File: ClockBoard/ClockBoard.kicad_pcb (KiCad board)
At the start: 2 copper layers, 43.2 x 55.9 mm, 25 parts, among them J1 Conn_01x03, J2 ClockBoard, J3 Mini USB, J4 USB Solder Pads, SW1 SW_Push, U1 ATMEGA328P, U2 UltimateGPSBreakout, U3 FT232RL, Y1 Crystal

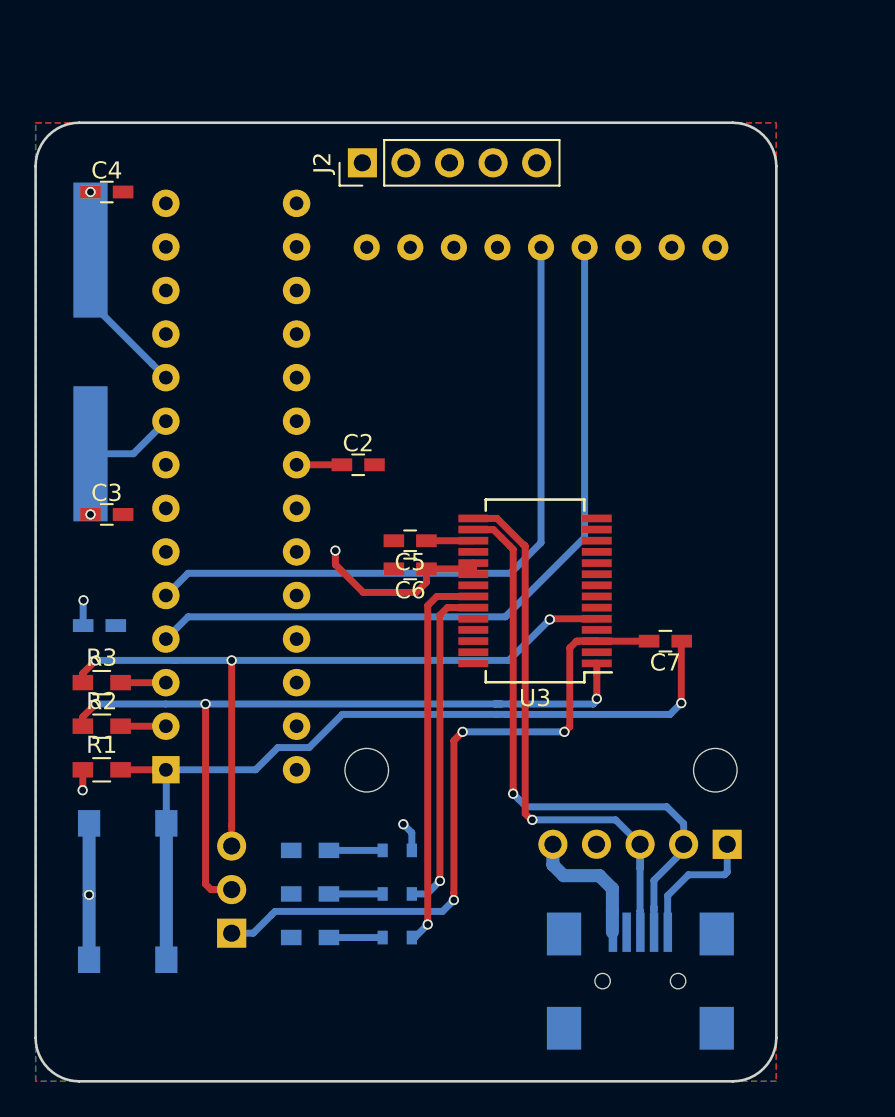
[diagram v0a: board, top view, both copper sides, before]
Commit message: Made Clock Board
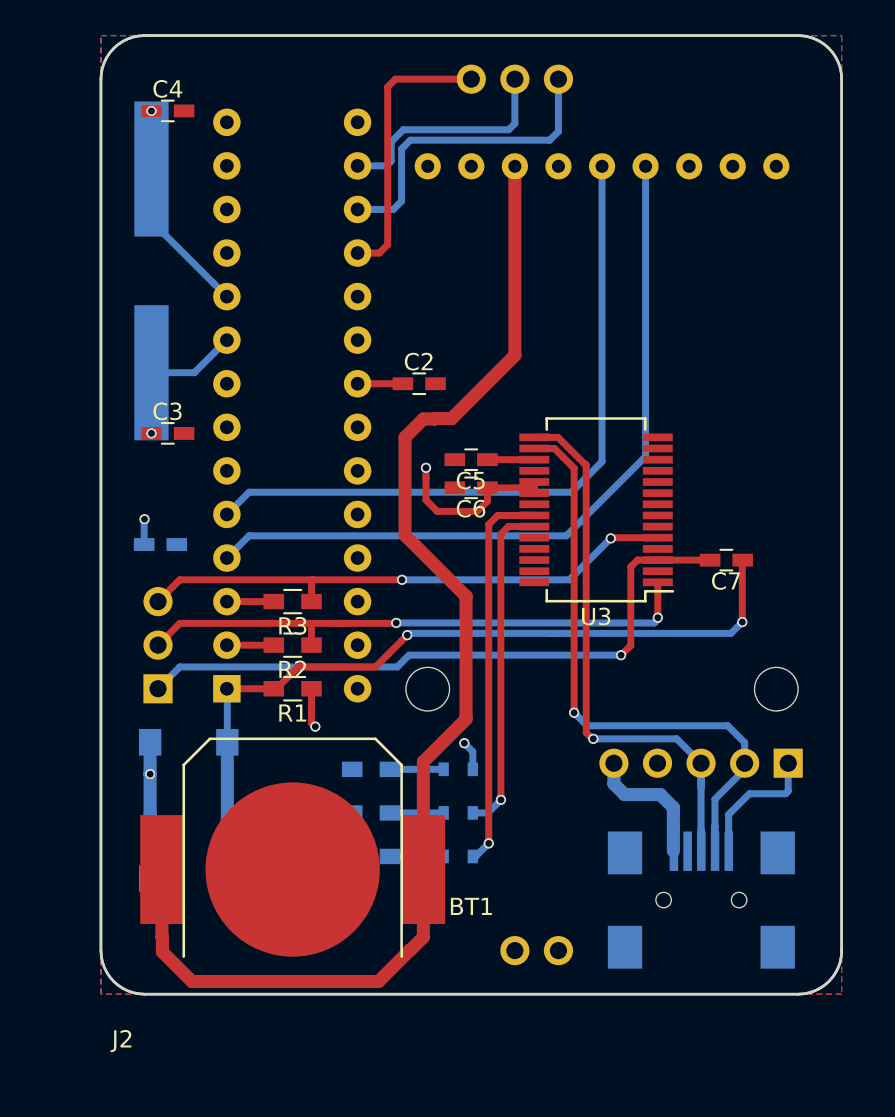
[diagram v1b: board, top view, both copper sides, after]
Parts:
- added BT1: Battery_Cell, Project_Library:CR1220_Battery_Holder, F.Cu at (126.7, 119.7)
- J2: footprint Pin_Headers:Pin_Header_Straight_1x05_Pitch2.54mm -> Project_Library:Clock_Board
- moved J2 50.8 mm to (123.2, 127.0), turned to 0 degrees
- moved J1 14.9 mm to (126.5, 109.2)
- moved R1 12.1 mm to (134.4, 109.2), turned to 180 degrees
- moved R2 12.1 mm to (134.4, 106.7), turned to 180 degrees
- moved R3 12.1 mm to (134.4, 104.1), turned to 180 degrees
- moved C5 5.91 mm to (144.8, 95.8)
- moved C7 5.91 mm to (159.6, 101.7)
- moved D2 5.91 mm to (144.0, 116.4)
- moved J3 5.91 mm to (158.2, 121.5)
- moved J4 5.91 mm to (163.3, 113.5)
- moved SW1 5.91 mm to (131.6, 113.3)
- moved U2 5.91 mm to (162.6, 78.7)
- moved C1 5.91 mm to (126.7, 100.8)
- moved C3 5.91 mm to (127.1, 94.3)
- moved C4 5.91 mm to (127.1, 75.5)
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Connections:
- U1 pad 16: (no net) -> CS
- U1 pad 17: (no net) -> CLK
- U1 pad 18: (no net) -> DIN
- U2 pad 3: (no net) -> VBat
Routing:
- net VBat: track 0.00 -> 72.9 mm
- net CLK: track 0.00 -> 18.4 mm
- net DIN: track 0.00 -> 16.2 mm
- net CS: track 0.00 -> 13.4 mm
- net IC_RX: track 45.7 -> 33.9 mm, vias 3 -> 2
- net IC_TX: track 42.6 -> 32.0 mm, vias 3 -> 2
- net Reset: track 49.0 -> 46.4 mm, vias 1 -> 2
- net RTS: track 39.5 -> 38.0 mm, vias 3 -> 1

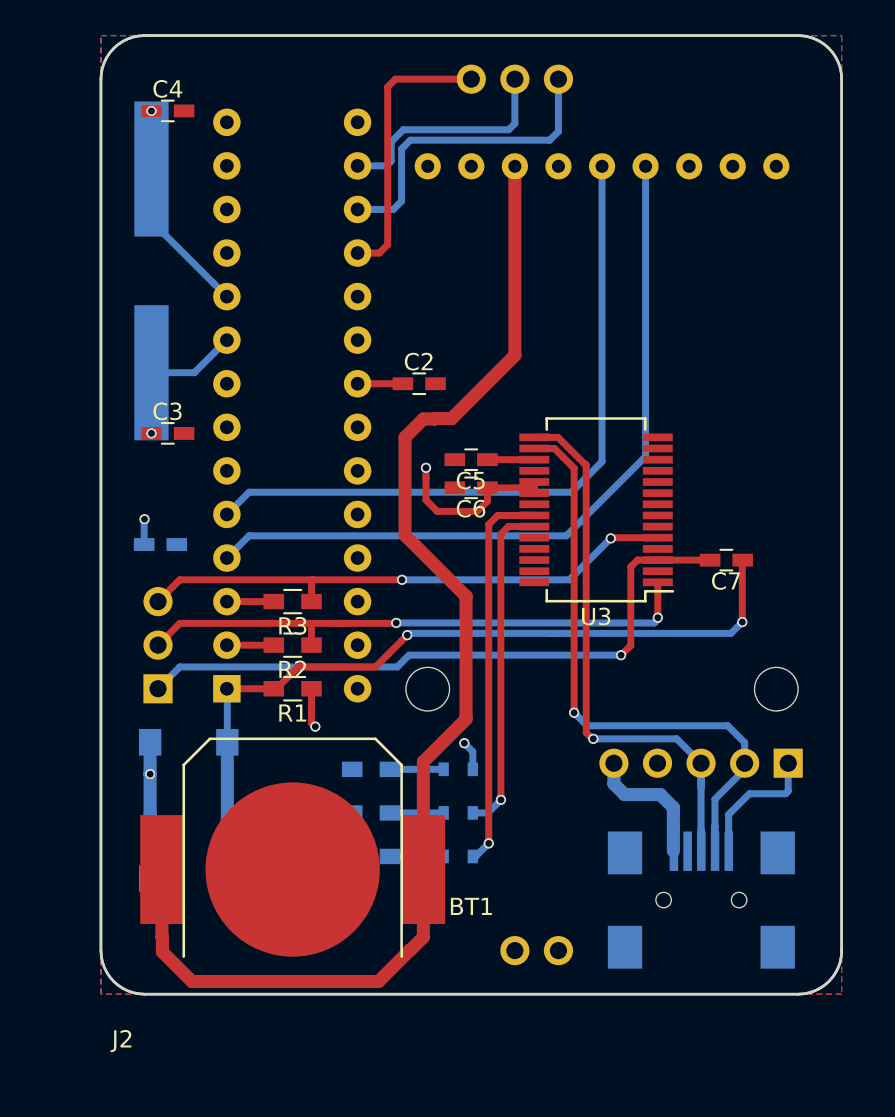
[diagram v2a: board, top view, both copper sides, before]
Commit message: Added silkscreen to boards and organized gerbs
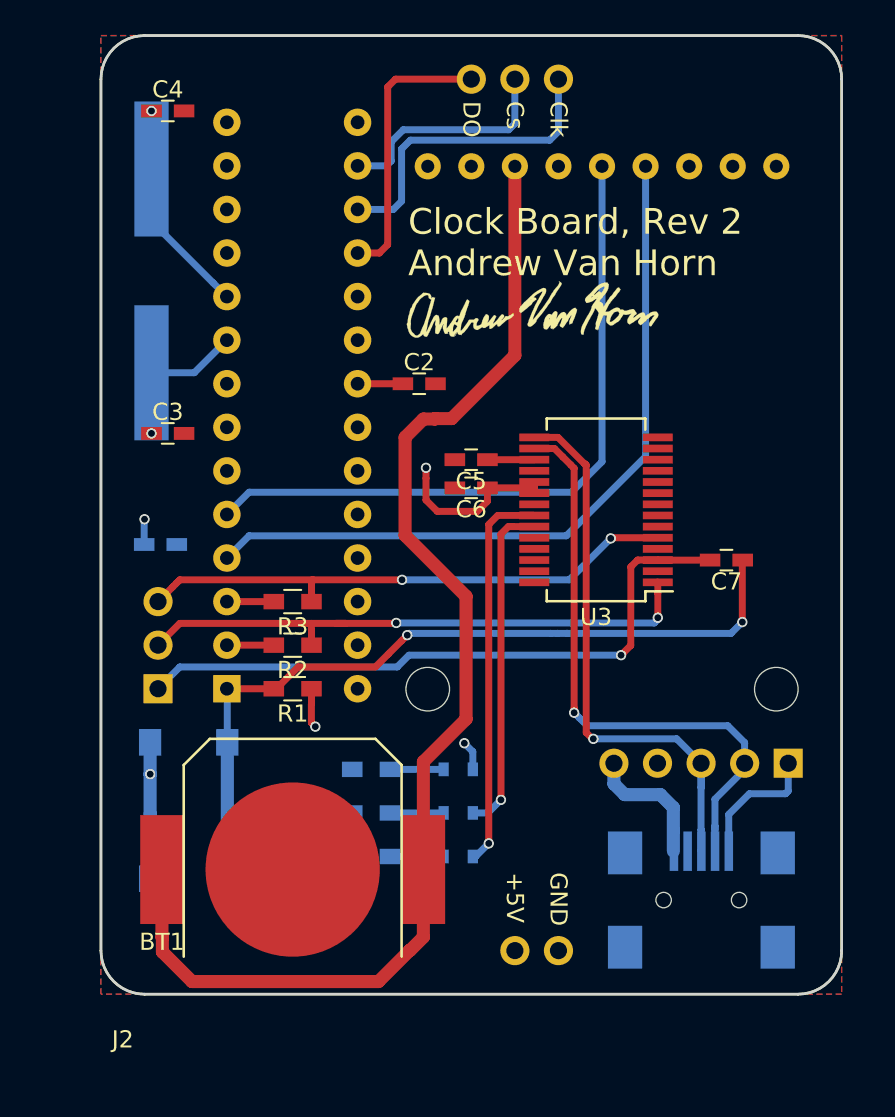
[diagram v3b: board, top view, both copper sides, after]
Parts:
- added G***: LOGO, MRDT_Silkscreens:z_sig_Andrew_Van_Horn_Sig_15mm, F.Cu at (148.3, 87.0)
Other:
- board text added: "+5V"
- board text added: "Clk"
- board text added: "Clock Board, Rev 2 Andrew Van Horn"
- board text added: "Cs"
- board text added: "DO"
- board text added: "GND"
